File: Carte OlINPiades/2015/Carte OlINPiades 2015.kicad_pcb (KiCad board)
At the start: 2 copper layers, 282 parts, among them U1 dsPIC33FJ128MC802, U2 LM7805, U3 LM2937-3.3

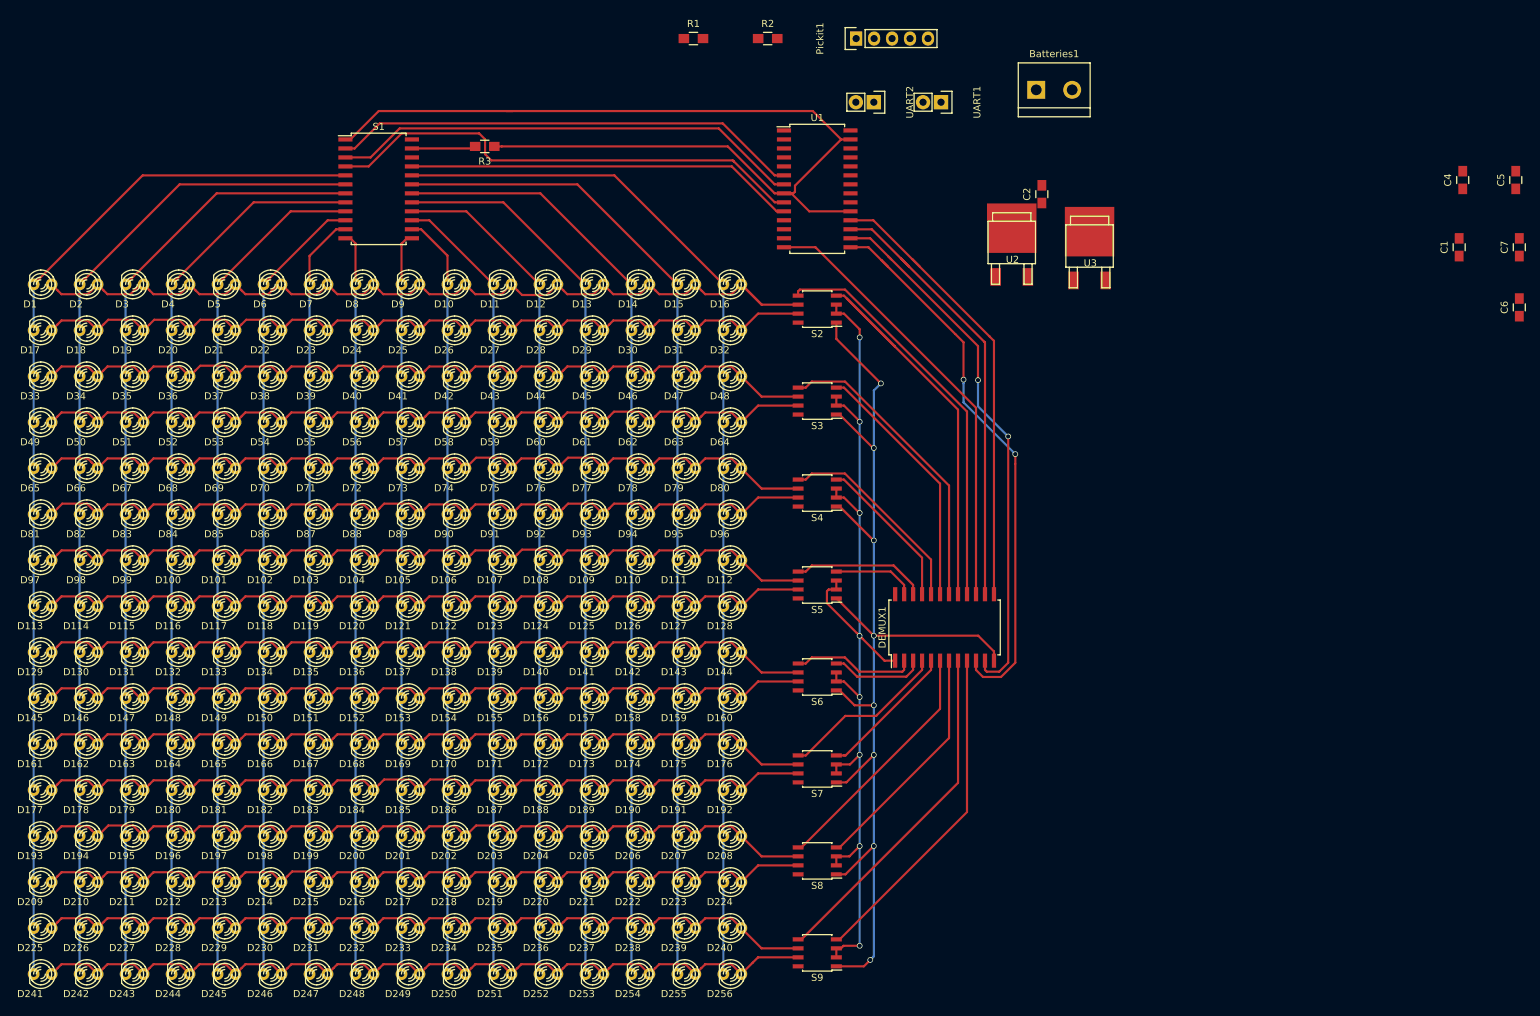
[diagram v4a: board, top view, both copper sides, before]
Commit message: manque partie alim
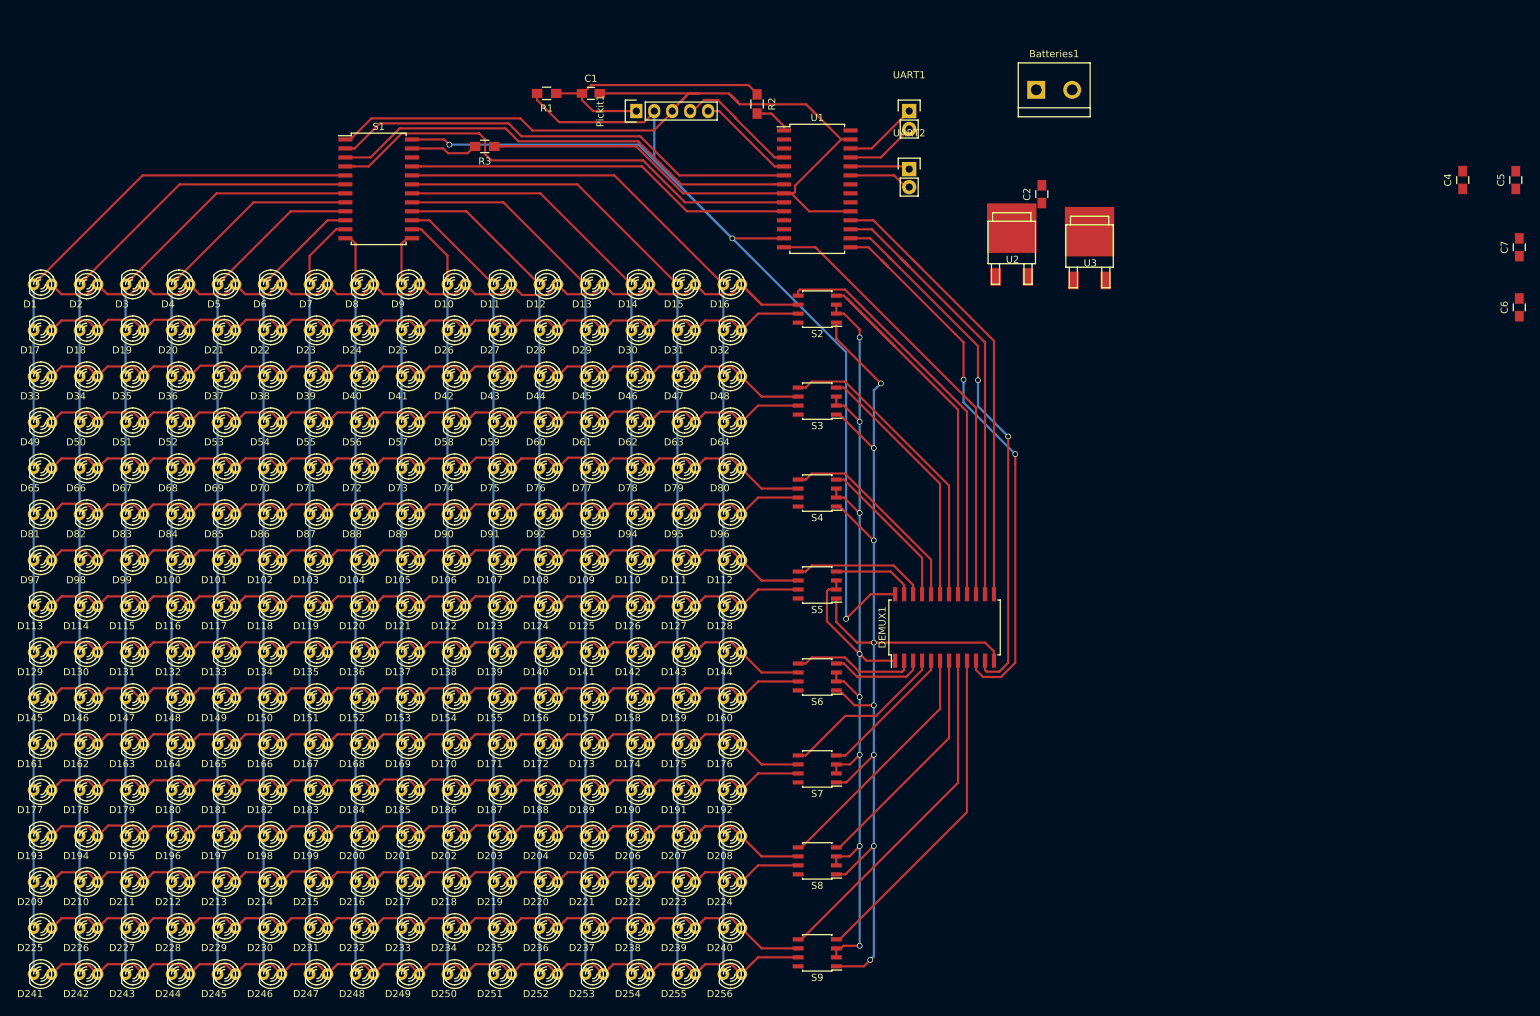
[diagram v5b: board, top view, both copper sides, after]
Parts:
- moved C1 124.7 mm to (125.0, 37.0), turned to 0 degrees
- moved Pickit1 32.7 mm to (131.4, 39.5)
- moved R1 22.2 mm to (118.8, 37.0), turned to 180 degrees
- moved UART2 10.7 mm to (170.0, 47.7), turned to 0 degrees
- moved R2 9.37 mm to (148.5, 38.5), turned to 270 degrees
- moved UART1 4.67 mm to (170.0, 39.5), turned to 0 degrees
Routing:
- net +3.3V: track 0.00 -> 170.3 mm, vias 0 -> 3
- net Net-(C1-Pad1): track 0.00 -> 38.7 mm
- net GND: track 301.9 -> 325.6 mm
- net PGD: track 0.00 -> 17.3 mm
- net PGC: track 0.00 -> 14.0 mm
- net RB15: track 0.00 -> 10.5 mm
- net RB14: track 0.00 -> 9.96 mm
- net RB12: track 0.00 -> 8.99 mm
- net RB13: track 0.00 -> 8.46 mm
- net Net-(R2-Pad2): track 0.00 -> 5.15 mm
- net +5V: track 141.6 -> 143.1 mm
- net Net-(R3-Pad2): track 9.07 -> 9.63 mm

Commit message: ajoute capa de découplage 2 ?
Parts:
- added C8: 0,1uF, Capacitors_SMD:C_0805_HandSoldering, F.Cu at (160.0, 62.0)
- added C9: 0,1uF, Capacitors_SMD:C_0805_HandSoldering, F.Cu at (161.2, 38.5)
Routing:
- net GND: track 325.6 -> 359.0 mm
- net +3.3V: track 170.3 -> 183.2 mm
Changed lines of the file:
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@@
 (kicad_pcb (version 4) (host pcbnew "(2015-09-09 BZR 6175)-product")
   (general
-    (links 597)
-    (no_connects 261)
+    (links 601)
+    (no_connects 243)
     (area 0 0 0 0)
     (thickness 1.6)
     (drawings 0)
-    (tracks 1390)
+    (tracks 1411)
     (zones 0)
-    (modules 282)
+    (modules 284)
     (nets 87)
   )
@@
     )
   )
+  (module Capacitors_SMD:C_0805_HandSoldering (layer F.Cu)
+    (at 160 62)
+    (descr "Capacitor SMD 0805, hand soldering")
+    (tags "capacitor 0805")
+    (attr smd)
+    (fp_text reference C8 (at 0 -2.1) (layer F.SilkS)
+      (effects (font (size 1 1) (thickness 0.15)))
+    )
+    (fp_text value 0,1uF (at 0 2.1) (layer F.Fab)
+      (effects (font (size 1 1) (thickness 0.15)))
+    )
+    (fp_line (start -2.3 -1) (end 2.3 -1) (layer F.CrtYd) (width 0.05))
+    (fp_line (start -2.3 1) (end 2.3 1) (layer F.CrtYd) (width 0.05))
+    (fp_line (start -2.3 -1) (end -2.3 1) (layer F.CrtYd) (width 0.05))
+    (fp_line (start 2.3 -1) (end 2.3 1) (layer F.CrtYd) (width 0.05))
+    (fp_line (start 0.5 -0.85) (end -0.5 -0.85) (layer F.SilkS) (width 0.15))
+    (fp_line (start -0.5 0.85) (end 0.5 0.85) (layer F.SilkS) (width 0.15))
+    (pad 1 smd rect (at -1.25 0) (size 1.5 1.25) (layers F.Cu F.Paste F.Mask)
+      (net 86 +3.3V))
+    (pad 2 smd rect (at 1.25 0) (size 1.5 1.25) (layers F.Cu F.Paste F.Mask)
+      (net 2 GND))
+    (model Capacitors_SMD.3dshapes/C_0805_HandSoldering.wrl
+      (at (xyz 0 0 0))
+      (scale (xyz 1 1 1))
+      (rotate (xyz 0 0 0))
+    )
+  )
+  (module Capacitors_SMD:C_0805_HandSoldering (layer F.Cu)
+    (at 161.25 38.5 180)
+    (descr "Capacitor SMD 0805, hand soldering")
+    (tags "capacitor 0805")
+    (attr smd)
+    (fp_text reference C9 (at 0 -2.1 180) (layer F.SilkS)
+      (effects (font (size 1 1) (thickness 0.15)))
+    )
+    (fp_text value 0,1uF (at 0 2.1 180) (layer F.Fab)
+      (effects (font (size 1 1) (thickness 0.15)))
+    )
+    (fp_line (start -2.3 -1) (end 2.3 -1) (layer F.CrtYd) (width 0.05))
+    (fp_line (start -2.3 1) (end 2.3 1) (layer F.CrtYd) (width 0.05))
+    (fp_line (start -2.3 -1) (end -2.3 1) (layer F.CrtYd) (width 0.05))
+    (fp_line (start 2.3 -1) (end 2.3 1) (layer F.CrtYd) (width 0.05))
+    (fp_line (start 0.5 -0.85) (end -0.5 -0.85) (layer F.SilkS) (width 0.15))
+    (fp_line (start -0.5 0.85) (end 0.5 0.85) (layer F.SilkS) (width 0.15))
+    (pad 1 smd rect (at -1.25 0 180) (size 1.5 1.25) (layers F.Cu F.Paste F.Mask)
+      (net 86 +3.3V))
+    (pad 2 smd rect (at 1.25 0 180) (size 1.5 1.25) (layers F.Cu F.Paste F.Mask)
+      (net 2 GND))
+    (model Capacitors_SMD.3dshapes/C_0805_HandSoldering.wrl
+      (at (xyz 0 0 0))
+      (scale (xyz 1 1 1))
+      (rotate (xyz 0 0 0))
+    )
+  )
+  (segment (start 161.25 62) (end 161.25 61.067) (width 0.308) (layer F.Cu) (net 2))
+  (segment (start 161.25 61.067) (end 153.854001 53.671001) (width 0.308) (layer F.Cu) (net 2))
+  (segment (start 153.854001 53.671001) (end 153.854001 51.381001) (width 0.308) (layer F.Cu) (net 2))
+  (segment (start 153.854001 51.381001) (end 153.608 51.135) (width 0.308) (layer F.Cu) (net 2))
+  (segment (start 153.608 51.135) (end 152.3 51.135) (width 0.308) (layer F.Cu) (net 2))
+  (segment (start 161.7 53.675) (end 160.392 53.675) (width 0.308) (layer F.Cu) (net 2))
+  (segment (start 160.145999 43.761001) (end 160.392 43.515) (width 0.308) (layer F.Cu) (net 2))
+  (segment (start 160.392 43.515) (end 161.7 43.515) (width 0.308) (layer F.Cu) (net 2))
+  (segment (start 160.392 53.675) (end 160.145999 53.428999) (width 0.308) (layer F.Cu) (net 2))
+  (segment (start 160.145999 53.428999) (end 160.145999 43.761001) (width 0.308) (layer F.Cu) (net 2))
+  (segment (start 160.392 53.675) (end 160.145999 53.921001) (width 0.308) (layer F.Cu) (net 2))
+  (segment (start 160.145999 53.921001) (end 160.145999 59.962999) (width 0.308) (layer F.Cu) (net 2))
+  (segment (start 160.145999 59.962999) (end 161.25 61.067) (width 0.308) (layer F.Cu) (net 2))
+  (segment (start 146.045999 38.545999) (end 150.911306 38.545999) (width 0.308) (layer F.Cu) (net 2))
+  (segment (start 150.911306 38.545999) (end 155.422999 38.545999) (width 0.308) (layer F.Cu) (net 2))
+  (segment (start 160 38.5) (end 158.942 38.5) (width 0.308) (layer F.Cu) (net 2))
+  (segment (start 158.942 38.5) (end 158.896001 38.545999) (width 0.308) (layer F.Cu) (net 2))
+  (segment (start 158.896001 38.545999) (end 150.911306 38.545999) (width 0.308) (layer F.Cu) (net 2))
   (segment (start 164.437637 114.643306) (end 165.003322 114.643306) (width 0.308) (layer F.Cu) (net 2))
   (segment (start 159.7 108.405) (end 159.7 111.719231) (width 0.308) (layer F.Cu) (net 2))
@@
   (segment (start 145.791361 38.291361) (end 146.045999 38.545999) (width 0.308) (layer F.Cu) (net 2))
   (segment (start 144.5 37) (end 145.791361 38.291361) (width 0.308) (layer F.Cu) (net 2))
-  (segment (start 146.045999 38.545999) (end 155.422999 38.545999) (width 0.308) (layer F.Cu) (net 2))
   (segment (start 155.422999 38.545999) (end 156.859818 39.982818) (width 0.308) (layer F.Cu) (net 2))
   (segment (start 136.5 39.3476) (end 138.5976 37.25) (width 0.308) (layer F.Cu) (net 2))
@@
   (segment (start 156.859818 39.982818) (end 158.205547 41.328547) (width 0.308) (layer F.Cu) (net 2))
   (segment (start 158.205547 41.328547) (end 160.392 43.515) (width 0.308) (layer F.Cu) (net 2))
-  (segment (start 160.392 43.515) (end 161.7 43.515) (width 0.308) (layer F.Cu) (net 2))
   (segment (start 153.854001 50.052999) (end 153.854001 50.888999) (width 0.308) (layer F.Cu) (net 2))
-  (segment (start 153.608 51.135) (end 152.3 51.135) (width 0.308) (layer F.Cu) (net 2))
   (segment (start 160.392 43.515) (end 153.854001 50.052999) (width 0.308) (layer F.Cu) (net 2))
   (segment (start 153.854001 50.888999) (end 153.608 51.135) (width 0.308) (layer F.Cu) (net 2))
-  (segment (start 161.7 53.675) (end 155.867202 53.675) (width 0.308) (layer F.Cu) (net 2))
-  (segment (start 155.867202 53.675) (end 153.327202 51.135) (width 0.308) (layer F.Cu) (net 2))
   (segment (start 153.327202 51.135) (end 152.3 51.135) (width 0.308) (layer F.Cu) (net 2))
   (segment (start 165 79) (end 165 87.134478) (width 0.308) (layer B.Cu) (net 2))
@@
   (segment (start 138.57748 53.675) (end 132.22748 47.325) (width 0.308) (layer F.Cu) (net 66))
   (segment (start 152.3 53.675) (end 138.57748 53.675) (width 0.308) (layer F.Cu) (net 66))
-  (segment (start 179.445 81.445) (end 156.755 58.755) (width 0.308) (layer F.Cu) (net 79))
-  (segment (start 156.755 58.755) (end 152.3 58.755) (width 0.308) (layer F.Cu) (net 79))
+  (segment (start 179.445 81.445) (end 161.771901 63.771901) (width 0.308) (layer F.Cu) (net 79))
+  (segment (start 152.3 58.755) (end 152.3 59.363) (width 0.308) (layer F.Cu) (net 79))
+  (segment (start 152.3 59.363) (end 156.708901 63.771901) (width 0.308) (layer F.Cu) (net 79))
+  (segment (start 156.708901 63.771901) (end 161.771901 63.771901) (width 0.308) (layer F.Cu) (net 79))
   (segment (start 179.445 107.8) (end 179.445 81.445) (width 0.308) (layer F.Cu) (net 79))
   (segment (start 161.7 48.595) (end 167.855798 48.595) (width 0.308) (layer F.Cu) (net 81))
@@
   (segment (start 159.7 79.865) (end 159.7 81.135) (width 0.308) (layer F.Cu) (net 85))
   (segment (start 159.7 68.135) (end 159.7 66.865) (width 0.308) (layer F.Cu) (net 85))
+  (segment (start 158.75 62) (end 158.75 61.067) (width 0.308) (layer F.Cu) (net 86))
+  (segment (start 158.75 61.067) (end 155.168 57.485) (width 0.308) (layer F.Cu) (net 86))
+  (segment (start 155.168 57.485) (end 153.608 57.485) (width 0.308) (layer F.Cu) (net 86))
+  (segment (start 153.608 57.485) (end 152.3 57.485) (width 0.308) (layer F.Cu) (net 86))
+  (segment (start 161.7 42.245) (end 161.7 39.3) (width 0.308) (layer F.Cu) (net 86))
+  (segment (start 161.7 39.3) (end 162.5 38.5) (width 0.308) (layer F.Cu) (net 86))
   (segment (start 161.477806 110.897521) (end 161.077807 111.29752) (width 0.308) (layer F.Cu) (net 86))
   (segment (start 161.077807 110.731835) (end 161.077807 111.29752) (width 0.308) (layer B.Cu) (net 86))

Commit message: remplacement du démux
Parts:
- DEMUX1: value 74HC4067 -> 74HC4514
- moved DEMUX1 0.30 mm to (175.0, 112.2)
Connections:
- DEMUX1 pad 1: +5V -> RB11
- DEMUX1 pad 10: RB6 -> Net-(DEMUX1-Pad10)
- DEMUX1 pad 11: RB7 -> Net-(DEMUX1-Pad11)
- DEMUX1 pad 13: RB9 -> Net-(DEMUX1-Pad13)
- DEMUX1 pad 14: RB8 -> Net-(DEMUX1-Pad14)
- DEMUX1 pad 15: RB5 -> Net-(DEMUX1-Pad15)
- DEMUX1 pad 2: Net-(DEMUX1-Pad2) -> RB6
- DEMUX1 pad 21: Net-(DEMUX1-Pad21) -> RB8
- DEMUX1 pad 22: Net-(DEMUX1-Pad22) -> RB9
- DEMUX1 pad 23: Net-(DEMUX1-Pad23) -> RB10
- DEMUX1 pad 3: Net-(DEMUX1-Pad3) -> RB7
- S2 pad 4: Net-(DEMUX1-Pad17) -> Net-(DEMUX1-Pad16)
- S2 pad 5: Net-(DEMUX1-Pad16) -> Net-(DEMUX1-Pad15)
- S3 pad 4: Net-(DEMUX1-Pad19) -> Net-(DEMUX1-Pad14)
- S3 pad 5: Net-(DEMUX1-Pad18) -> Net-(DEMUX1-Pad13)
- S4 pad 4: Net-(DEMUX1-Pad21) -> Net-(DEMUX1-Pad20)
- S4 pad 5: Net-(DEMUX1-Pad20) -> Net-(DEMUX1-Pad19)
- S5 pad 4: Net-(DEMUX1-Pad23) -> Net-(DEMUX1-Pad18)
- S5 pad 5: Net-(DEMUX1-Pad22) -> Net-(DEMUX1-Pad17)
- S6 pad 4: Net-(DEMUX1-Pad3) -> Net-(DEMUX1-Pad5)
- S6 pad 5: Net-(DEMUX1-Pad2) -> Net-(DEMUX1-Pad4)
- S7 pad 4: Net-(DEMUX1-Pad5) -> Net-(DEMUX1-Pad7)
- S7 pad 5: Net-(DEMUX1-Pad4) -> Net-(DEMUX1-Pad6)
- S8 pad 4: Net-(DEMUX1-Pad7) -> Net-(DEMUX1-Pad10)
- S8 pad 5: Net-(DEMUX1-Pad6) -> Net-(DEMUX1-Pad8)
- S9 pad 4: Net-(DEMUX1-Pad9) -> Net-(DEMUX1-Pad11)
- S9 pad 5: Net-(DEMUX1-Pad8) -> Net-(DEMUX1-Pad9)
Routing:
- net RB11: track 0.00 -> 95.5 mm
- net RB10: track 0.00 -> 94.3 mm
- net Net-(DEMUX1-Pad15): track 0.00 -> 63.6 mm
- net RB5: track 63.3 -> 0.00 mm
- net Net-(DEMUX1-Pad11): track 0.00 -> 48.4 mm
- net Net-(DEMUX1-Pad13): track 0.00 -> 47.9 mm
- net Net-(DEMUX1-Pad14): track 0.00 -> 38.2 mm
- net Net-(DEMUX1-Pad10): track 0.00 -> 35.3 mm
- net Net-(DEMUX1-Pad17): track 59.6 -> 27.8 mm, vias 0 -> 2
- net Net-(DEMUX1-Pad18): track 43.1 -> 19.5 mm, vias 0 -> 2
- net Net-(DEMUX1-Pad21): track 21.9 -> 0.00 mm
- net RB9: track 64.6 -> 86.4 mm
- net RB8: track 62.9 -> 82.2 mm
- net Net-(DEMUX1-Pad22): track 19.1 -> 0.00 mm
- net Net-(DEMUX1-Pad2): track 17.6 -> 0.00 mm
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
